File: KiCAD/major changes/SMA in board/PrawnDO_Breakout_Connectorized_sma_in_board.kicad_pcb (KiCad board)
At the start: 2 copper layers, 113 x 86.8 mm, 81 parts, among them IC1 74LVT245D,118, IC2 74LVT245D,118, IC3 74LVT245D,118, IC4 74LVT245D,118, J1 do15, J10 do6, J11 do5, J12 do4, J13 do3, J14 do2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

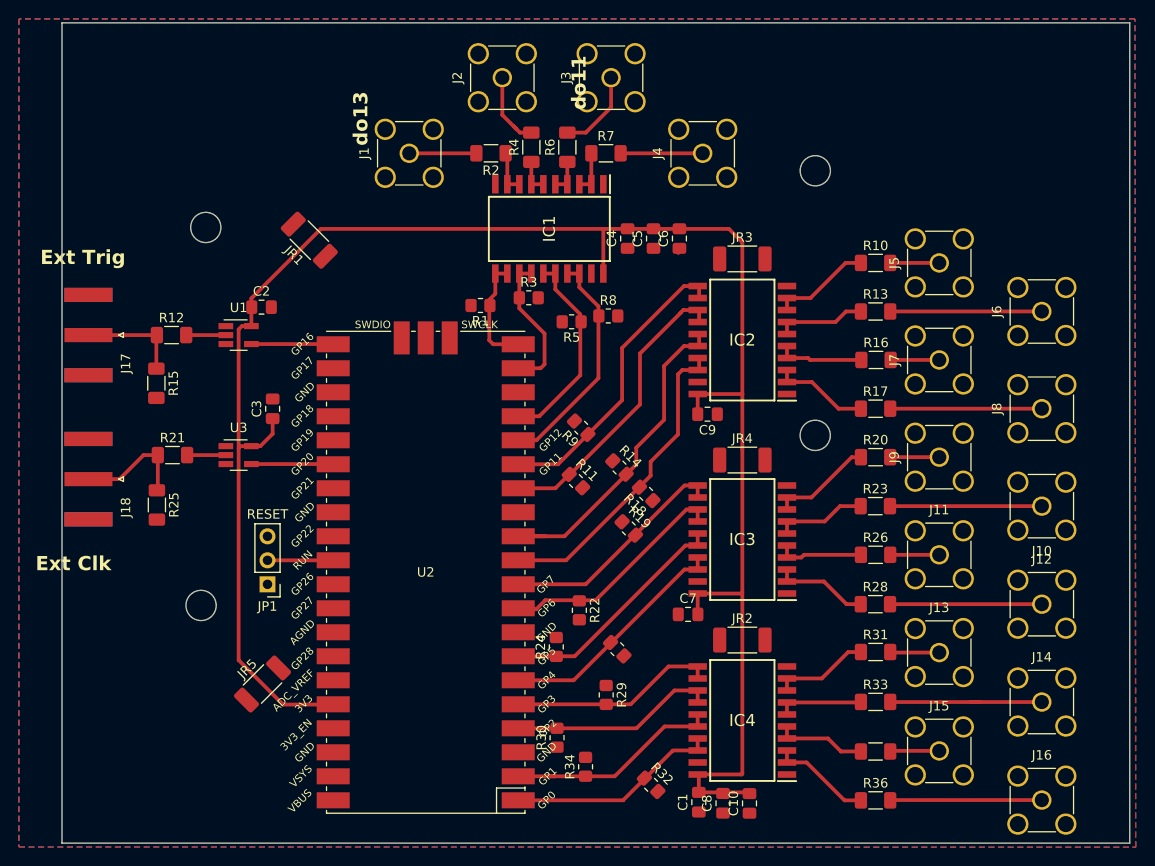
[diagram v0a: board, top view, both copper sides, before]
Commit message: Moved components, added headers, changed transmission track widths, moved mounting hole placement
Changed Capacitor footprints from 0806 to 1210
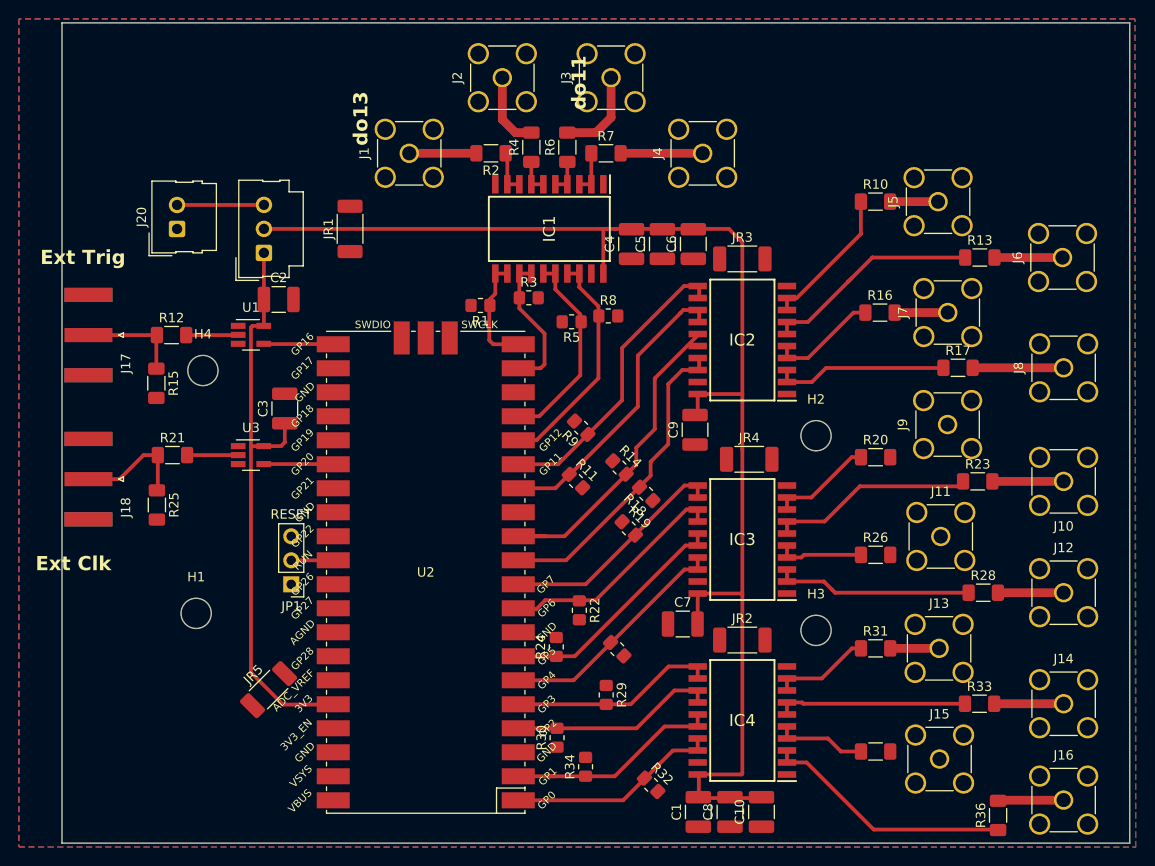
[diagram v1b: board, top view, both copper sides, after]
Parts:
- removed REF** (x4): MountingHole_3.2mm_M3_ISO7380, MountingHole:MountingHole_3.2mm_M3_ISO7380
- added H1: MountingHole, MountingHole:MountingHole_3.2mm_M3_ISO7380, F.Cu at (86.1, 116.7)
- added H2: MountingHole, MountingHole:MountingHole_3.2mm_M3_ISO7380, F.Cu at (151.7, 97.9)
- added H3: MountingHole, MountingHole:MountingHole_3.2mm_M3_ISO7380, F.Cu at (151.7, 118.5)
- added H4: MountingHole, MountingHole:MountingHole_3.2mm_M3_ISO7380, F.Cu at (86.8, 91.0)
- added J19: Conn_01x03, Connector_Molex:Molex_SL_171971-0003_1x03_P2.54mm_Vertical, F.Cu at (93.3, 78.5)
- added J20: Conn_01x02, Connector_Molex:Molex_SL_171971-0002_1x02_P2.54mm_Vertical, F.Cu at (84.1, 76.0)
- C1, C10, C2, C3, C4, C5, C6, C7, C8, C9: footprint Capacitor_SMD:C_0805_2012Metric_Pad1.18x1.45mm_HandSolder -> Capacitor_SMD:C_1210_3225Metric_Pad1.33x2.70mm_HandSolder
- moved R36 13.1 mm to (171.0, 138.1), turned to 90 degrees
- moved R13 12.4 mm to (169.0, 79.0)
- moved R28 11.5 mm to (169.4, 114.5)
- moved R23 11.1 mm to (168.8, 102.7)
- moved R33 11.0 mm to (169.0, 126.2)
- moved R17 9.74 mm to (166.7, 90.7)
- moved R10 6.49 mm to (158.0, 73.1)
- moved J5 6.48 mm to (164.6, 73.1)
- moved J6 6.11 mm to (177.8, 79.0)
- moved J7 5.10 mm to (165.6, 84.9)
- moved R16 5.03 mm to (158.5, 84.9)
- moved J8 4.90 mm to (177.9, 90.7)
- moved JR1 4.47 mm to (102.4, 76.0), turned to 90 degrees
- moved J9 3.56 mm to (165.6, 96.7)
- moved J10 3.49 mm to (177.9, 102.7)
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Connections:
- C1 pad 2: 3_3V_Pico -> Power  Supply
- C10 pad 2: 3_3V_Pico -> Power  Supply
- C4 pad 2: 3_3V_Pico -> Power  Supply
- C5 pad 2: 3_3V_Pico -> Power  Supply
- C6 pad 2: 3_3V_Pico -> Power  Supply
- C7 pad 2: 3_3V_Pico -> Power  Supply
- C8 pad 2: 3_3V_Pico -> Power  Supply
- C9 pad 2: 3_3V_Pico -> Power  Supply
- IC1 pad 20: 3_3V_Pico -> Power  Supply
- IC2 pad 20: 3_3V_Pico -> Power  Supply
- IC3 pad 20: 3_3V_Pico -> Power  Supply
- IC4 pad 20: 3_3V_Pico -> Power  Supply
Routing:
- net Power  Supply: track 0.00 -> 140.9 mm
- net 3_3V_Pico: track 200.7 -> 62.6 mm
- net Net-(IC4A-A0): track 10.9 -> 26.6 mm
- net Net-(IC2A-A4): track 9.56 -> 23.6 mm
- net Net-(IC3A-A4): track 9.74 -> 21.7 mm
- net Net-(IC3A-A0): track 10.1 -> 21.5 mm
- net Net-(IC4A-A4): track 9.12 -> 20.4 mm
- net do2: track 17.4 -> 7.71 mm
- net do0: track 16.3 -> 7.01 mm
- net do4: track 16.2 -> 6.95 mm
- net Ext. Power: track 0.00 -> 9.20 mm
- net do10: track 16.1 -> 7.20 mm
- net do6: track 16.3 -> 7.54 mm
- net Net-(IC2A-A0): track 10.3 -> 18.4 mm
- net do8: track 16.3 -> 9.62 mm
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
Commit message: Spaced out the SMAs a bit more
made sure the DRC didn't throw any major flags
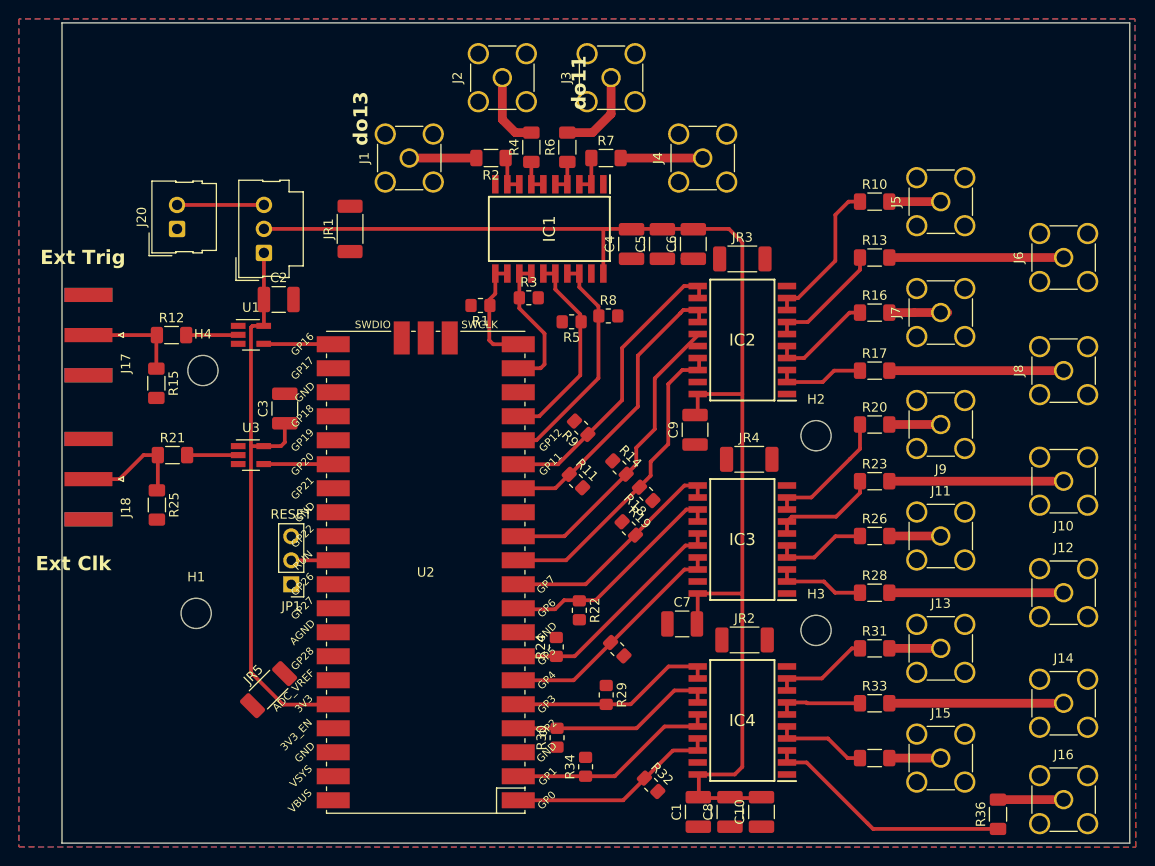
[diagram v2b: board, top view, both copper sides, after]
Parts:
- moved R28 11.5 mm to (157.9, 114.5)
- moved R13 11.1 mm to (157.9, 79.0)
- moved R33 11.1 mm to (157.9, 126.2)
- moved R23 10.9 mm to (157.9, 102.7)
- moved R17 8.83 mm to (157.9, 91.0)
- moved R20 3.46 mm to (157.9, 96.7)
- moved R26 1.99 mm to (157.9, 108.5)
- moved J7 0.74 mm to (164.9, 84.9)
- moved J9 0.72 mm to (164.9, 96.7), turned to 180 degrees
- moved R35 0.70 mm to (157.9, 132.0)
- moved R16 0.57 mm to (157.9, 84.9)
- moved J1 0.50 mm to (108.7, 68.5)
- moved J4 0.50 mm to (139.7, 68.5)
- moved R2 0.50 mm to (117.3, 68.5)
- moved R7 0.50 mm to (129.5, 68.5)
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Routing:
- net Net-(IC3A-A0): track 21.5 -> 9.49 mm
- net do4: track 6.95 -> 18.5 mm
- net Net-(IC4A-A4): track 20.4 -> 9.03 mm
- net do10: track 7.20 -> 18.5 mm
- net Net-(IC2A-A4): track 23.6 -> 12.6 mm
- net do6: track 7.54 -> 18.5 mm
- net do2: track 7.71 -> 18.5 mm
- net Net-(IC3A-A4): track 21.7 -> 11.5 mm
- net Net-(IC2A-A0): track 18.4 -> 9.49 mm
- net do8: track 9.62 -> 18.5 mm
- net do7: track 0.00 -> 5.46 mm
- net do5: track 0.02 -> 5.45 mm
- net do1: track 0.09 -> 5.45 mm
- net Net-(IC2A-B2): track 36.9 -> 33.1 mm
- net Net-(IC3A-A6): track 10.9 -> 13.7 mm
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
